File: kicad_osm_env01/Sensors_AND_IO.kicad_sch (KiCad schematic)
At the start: 51 parts

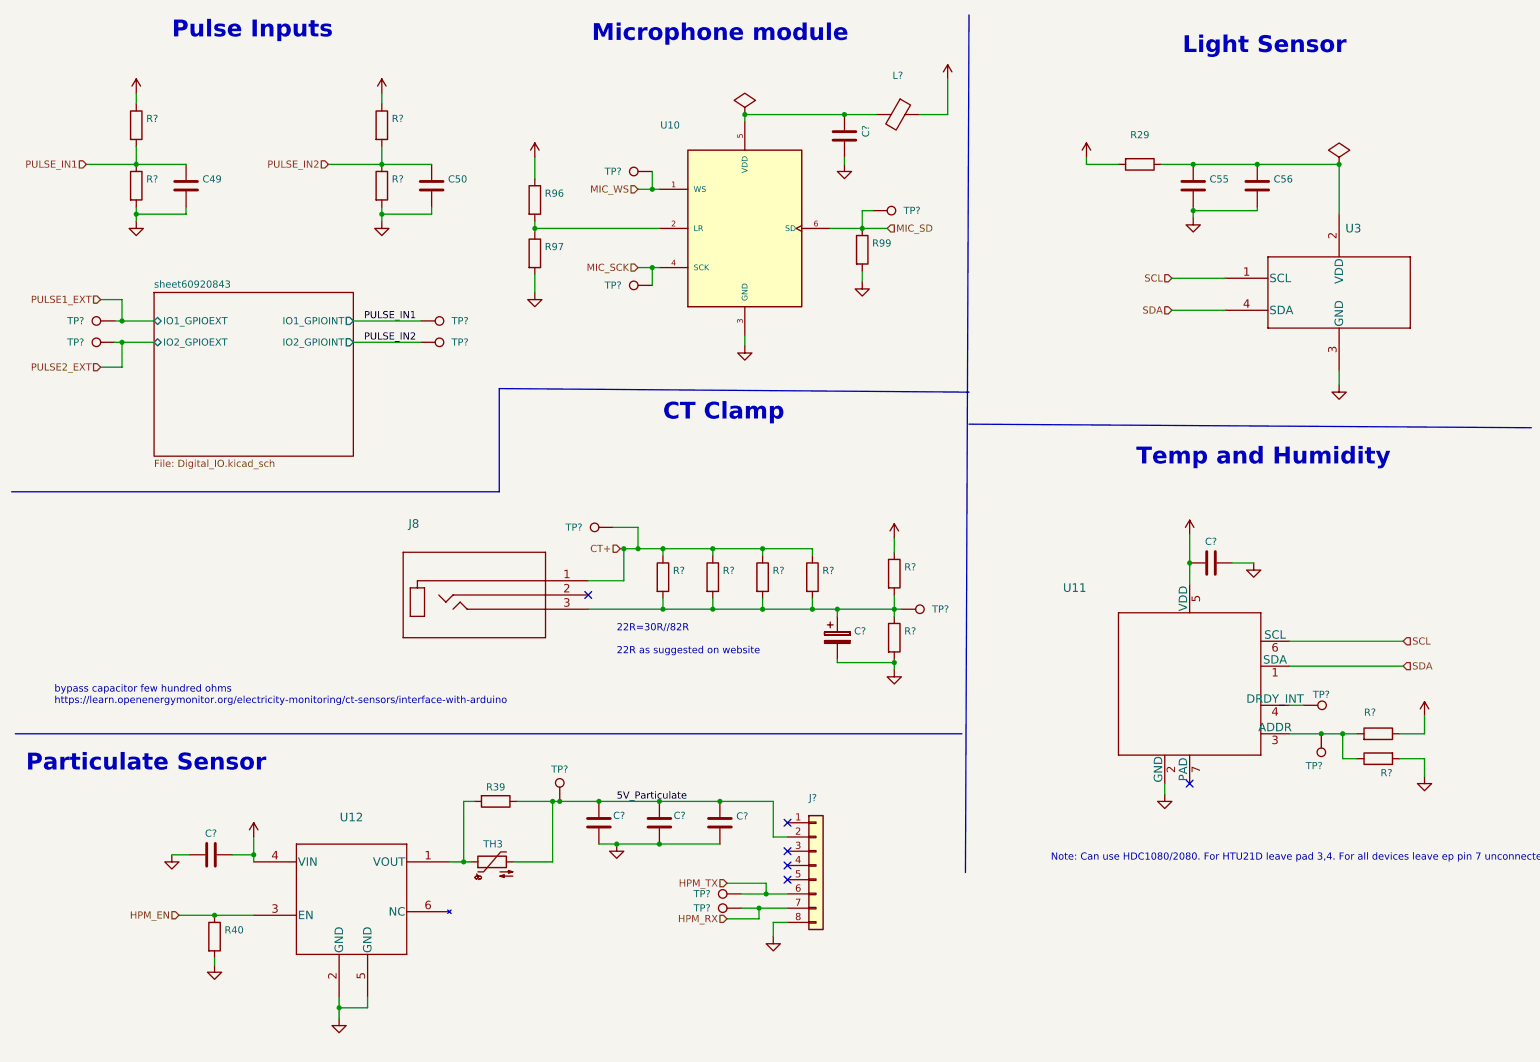
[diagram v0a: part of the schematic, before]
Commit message: added stml433 to schematic and carried out some mods
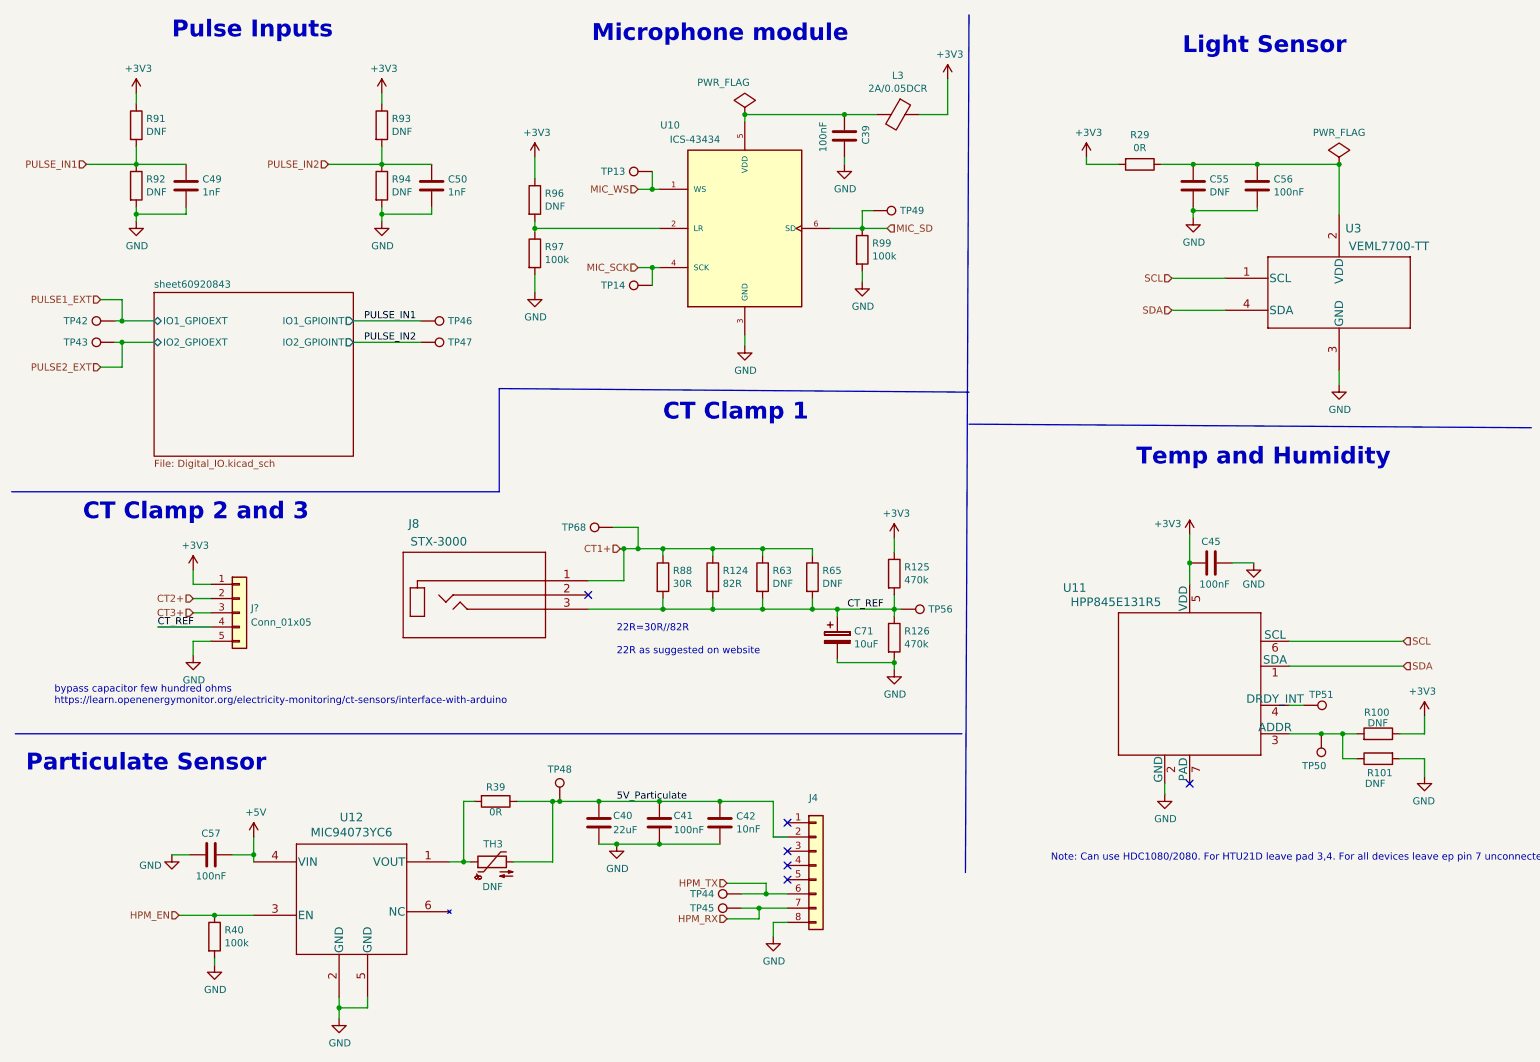
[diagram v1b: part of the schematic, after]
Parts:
- added J?: Conn_01x05, symbol Connector:Conn_01x05
- C39, C41, C45, C57: renamed from C?; value (none) -> 100nF; footprint (none) -> Capacitor_SMD:C_0402_1005Metric
- C40: renamed from C?; value (none) -> 22uF; footprint (none) -> Capacitor_SMD:C_0805_2012Metric
- C42: renamed from C?; value (none) -> 10nF; footprint (none) -> Capacitor_SMD:C_0402_1005Metric
- C49, C50: value (none) -> 1nF; footprint (none) -> Capacitor_SMD:C_0402_1005Metric
- C55: value (none) -> DNF; footprint (none) -> Capacitor_SMD:C_0603_1608Metric
- C56: value (none) -> 100nF; footprint (none) -> Capacitor_SMD:C_0402_1005Metric
- C71: renamed from C?; value (none) -> 10uF; footprint (none) -> Capacitor_SMD:CP_Elec_4x5.4
- J4: renamed from J?; value (none) -> Conn_01x08; footprint (none) -> Connector_Molex:Molex_PicoBlade_53047-0810_1x08_P1.25mm_Vertical
- J8: value (none) -> STX-3000; footprint (none) -> Devtank_PCB_lib:STX-3000
- L3: renamed from L?; value (none) -> 2A/0.05DCR; footprint (none) -> Inductor_SMD:L_0402_1005Metric
- R100, R101, R91, R92, R93, R94: renamed from R?; value (none) -> DNF; footprint (none) -> Resistor_SMD:R_0603_1608Metric
- R124: renamed from R?; value (none) -> 82R; footprint (none) -> Resistor_SMD:R_1206_3216Metric
- R125, R126: renamed from R?; value (none) -> 470k; footprint (none) -> Resistor_SMD:R_0603_1608Metric
- R29, R39: value (none) -> 0R; footprint (none) -> Resistor_SMD:R_0603_1608Metric
- R40, R97, R99: value (none) -> 100k; footprint (none) -> Resistor_SMD:R_0603_1608Metric
- R63, R65: renamed from R?; value (none) -> DNF; footprint (none) -> Resistor_SMD:R_1206_3216Metric
- R88: renamed from R?; value (none) -> 30R; footprint (none) -> Resistor_SMD:R_1206_3216Metric
- R96: value (none) -> DNF; footprint (none) -> Resistor_SMD:R_0603_1608Metric
- TH3: value (none) -> DNF; footprint (none) -> Resistor_THT:R_Axial_DIN0617_L17.0mm_D6.0mm_P5.08mm_Vertical
- TP13, TP14, TP48, TP49: renamed from TP?; value (none) -> Test_Point; footprint (none) -> TestPoint:TestPoint_THTPad_D1.0mm_Drill0.5mm
- TP42, TP43, TP44, TP45, TP46, TP47, TP50, TP51, TP56, TP68: renamed from TP?; value (none) -> Test_Point; footprint (none) -> TestPoint:TestPoint_Pad_D1.5mm
- U10: value (none) -> ICS-43434; footprint (none) -> Devtank_PCB_lib:ICS-43434
- U11: value (none) -> HPP845E131R5; footprint (none) -> Devtank_PCB_lib:HPP845E131R5_temperature_humidity_sensor
- U12: value (none) -> MIC94073YC6; footprint (none) -> Package_TO_SOT_SMD:SOT-363_SC-70-6
- U3: value (none) -> VEML7700-TT; footprint (none) -> Devtank_PCB_lib:VEML7700-TT
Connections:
- net +3V3: now also J?.1 (Pin_1)
- net GND: now also J?.5 (Pin_5)
- net CT_REF: now reaches C71.1, J8.3, R124.2, R125.2, R126.1, R63.2, R65.2, R88.2, TP56.1
- net CT_REF: now also J?.4 (Pin_4)
- net CT+ renamed CT1+
- new net CT2+: J?.2 (Pin_2)
- new net CT3+: J?.3 (Pin_3)
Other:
- note added: "CT Clamp 1"
- note added: "CT Clamp 2 and 3"
- note removed: "CT Clamp"

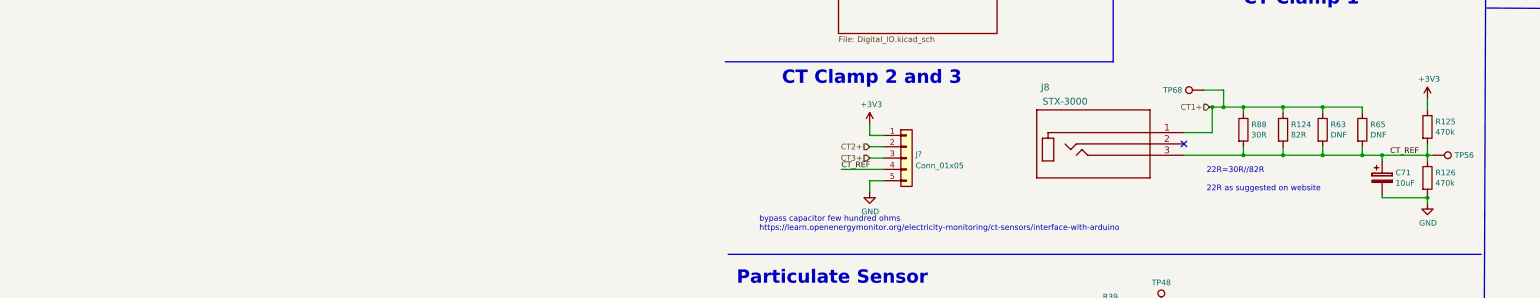
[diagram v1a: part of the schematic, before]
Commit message: updated mod list
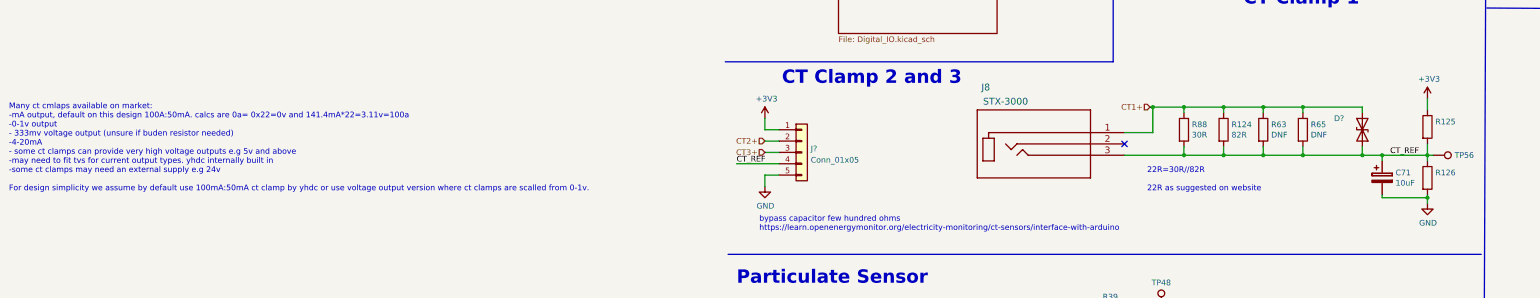
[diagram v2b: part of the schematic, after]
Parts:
- removed TP68: Test_Point, TestPoint:TestPoint_Pad_D1.5mm, symbol OSM_env01-rescue:Test_Point-Connector-ESP32-EVB_Rev_D-rescue
- added D?: (no value), Diode_SMD:D_SOD-123, symbol device:D_TVS
- R125, R126: value 470k -> (none)
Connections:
- net CT1+: now also D?.1 (A1)
- net CT_REF: now also D?.2 (A2)
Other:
- note added: "Many ct cmlaps available on market: -mA output, default on this design 100A:50mA. calcs are 0a= 0x22=0v and 141.4mA*22=3.11v=100a -0-1v output - 333mv voltage output (unsure if buden resistor needed) -4-20mA - some ct clamps can provide very high voltage outputs e.g 5v and above -may need to fit tvs for current output types. yhdc internally built in -some ct clamps may need an external supply e.g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"
- moved on the sheet: J8, J?, R124, R63, R65, R88

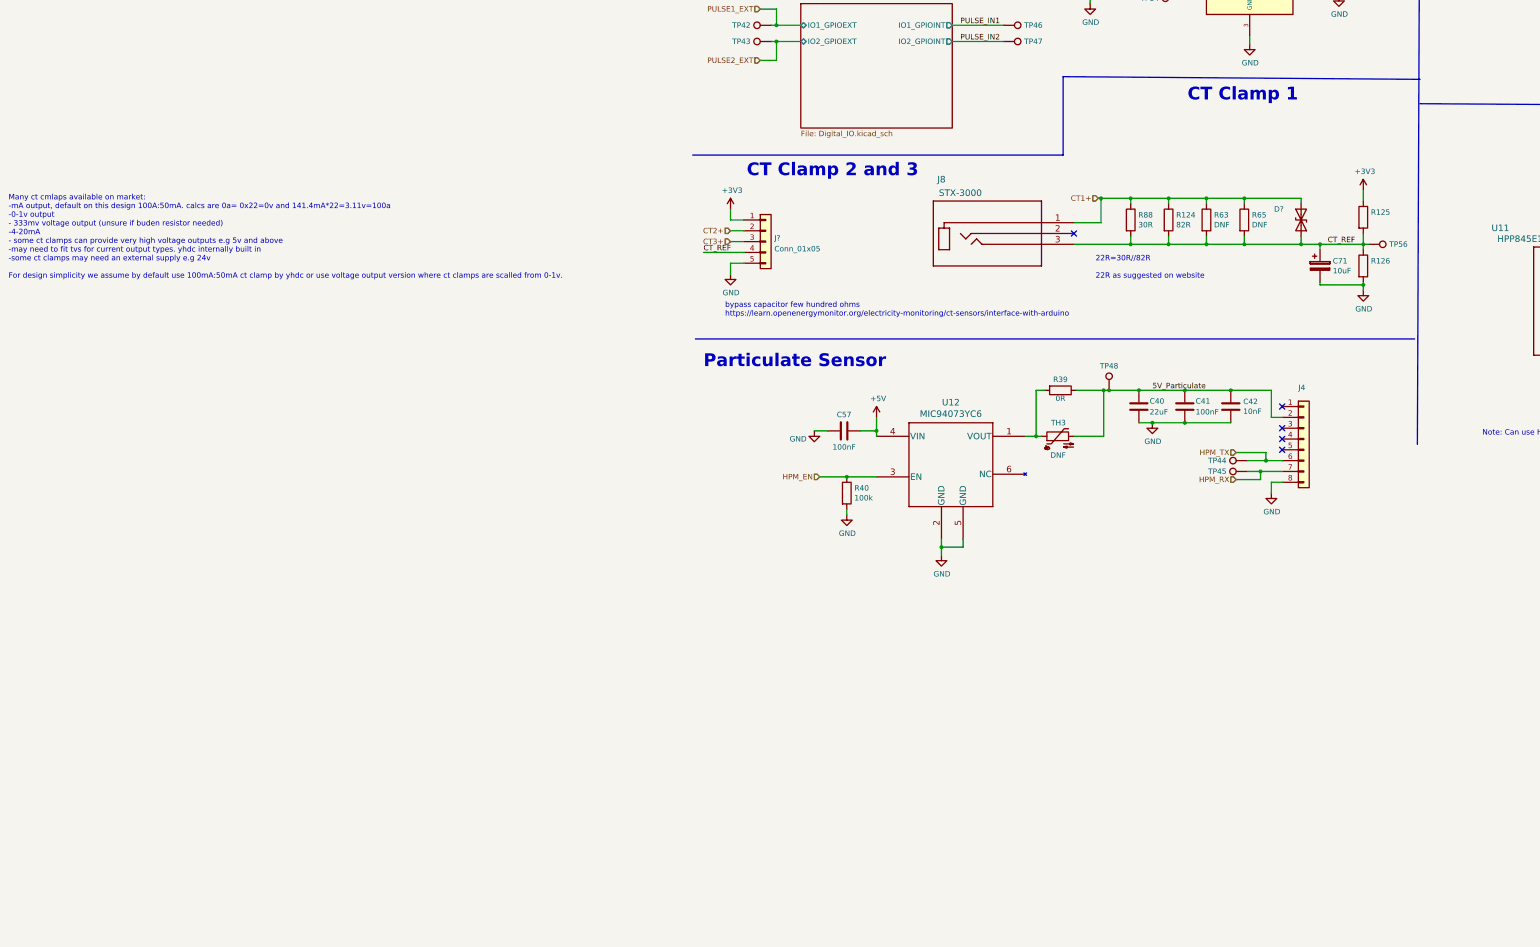
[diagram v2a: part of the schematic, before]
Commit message: updated schematics
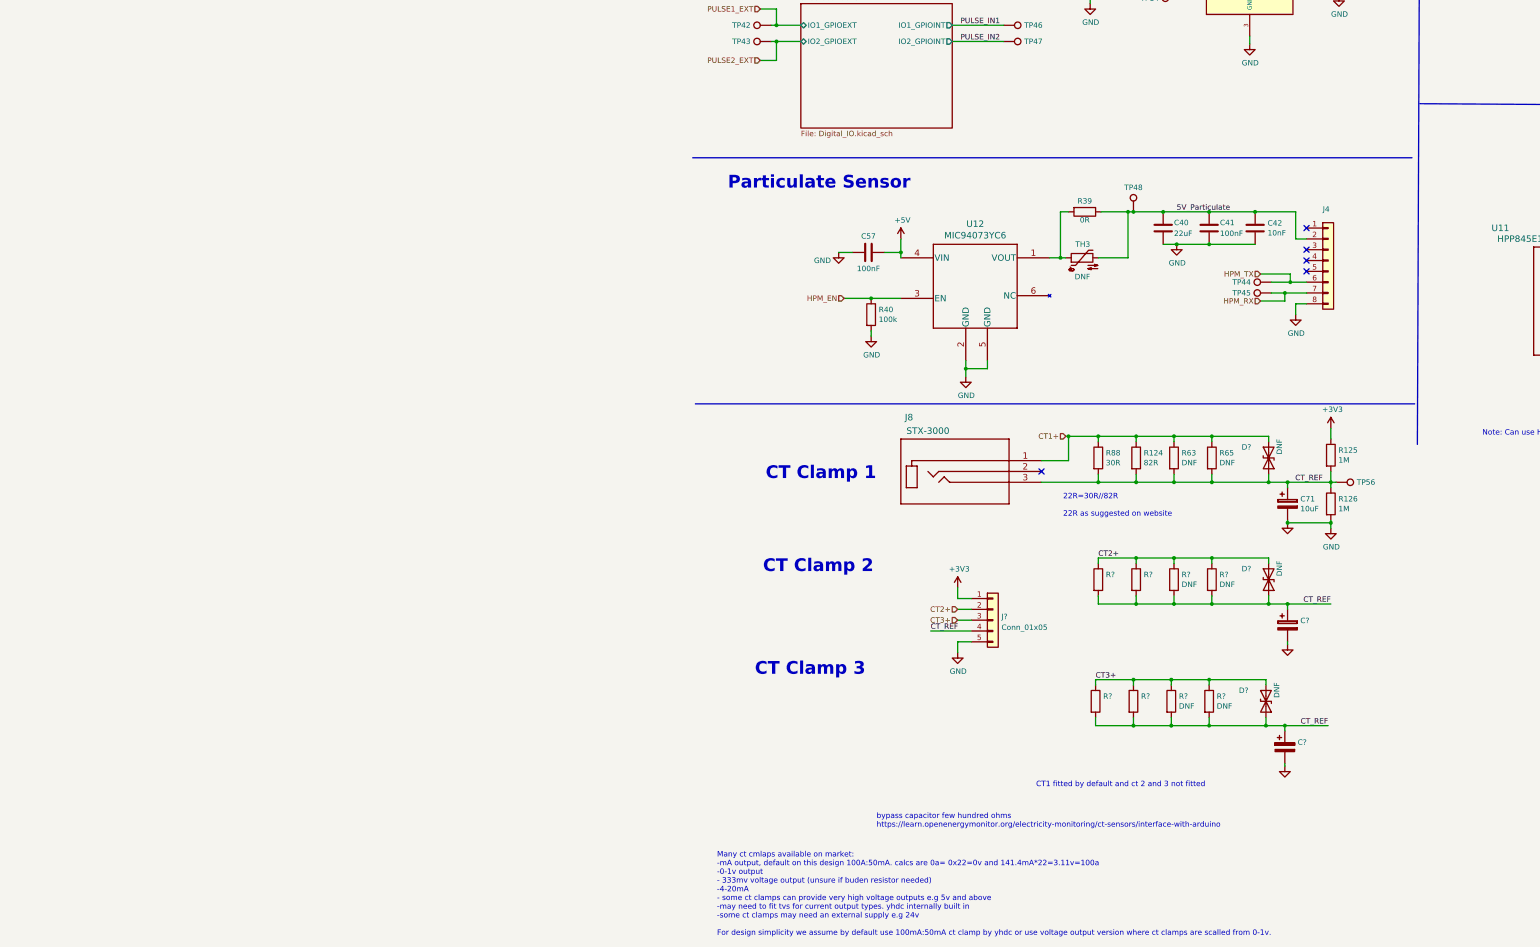
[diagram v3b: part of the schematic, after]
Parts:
- added C?: (no value), Capacitor_SMD:CP_Elec_4x5.4, symbol device:CP
- added C?: ~, Capacitor_SMD:CP_Elec_4x5.4, symbol device:CP
- added D? (x2): DNF, Diode_SMD:D_SOD-123, symbol device:D_TVS
- added R? (x2): (no value), Resistor_SMD:R_1206_3216Metric, symbol device:R
- added R? (x4): DNF, Resistor_SMD:R_1206_3216Metric, symbol device:R
- added R? (x2): ~, Resistor_SMD:R_1206_3216Metric, symbol device:R
- D?: value (none) -> DNF
- R125, R126: value (none) -> 1M
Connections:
- net CT2+: now also D?.1 (A1), R?.1, R?.1, R?.1, R?.1
- net CT3+: now also D?.1 (A1), R?.1, R?.1, R?.1, R?.1
- net CT_REF: now also C?.1, C?.1, D?.2 (A2), D?.2 (A2), R?.2, R?.2, R?.2, R?.2, R?.2, R?.2, R?.2, R?.2
- net GND: now also C?.2, C?.2
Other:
- note added: "CT Clamp 2"
- note added: "CT Clamp 3"
- note added: "CT1 fitted by default and ct 2 and 3 not fitted"
- note removed: "CT Clamp 2 and 3"
- moved on the sheet: C40, C41, C42, C57, C71, D?, J4, J8, J?, R124, R125, R126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
